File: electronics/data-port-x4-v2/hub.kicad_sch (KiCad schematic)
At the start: 41 parts, among them J1 LEAD, Q1 2N7002, Q2 2N7002, Q3 2N7002, U1 USB2517I-JZX, U2 TCA6408ARGTR, U3 AP2114H-3.3TRG1, U4 H5VU25UC, U6 TCA6408ARGTR, Y1 X322524MSB4SI

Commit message: DATA x4 v2: D2 holds the co-processor in reset with the hub (schematic review S2)
With CFG_SEL 000 the USB2517 samples each downstream D+ / D- as a
port-disable strap when RESET_N rises, and one high line disables the
port (DS00001598C Table 5-1 p.10, checked by the user): the RP2354B's
D+ pull-up on port 5 must not be up by then.

- D2, one Schottky of a BAT54S (C7420333, preferred, no fee; VF <= 240 mV
  at 0.1 mA, <= 320 mV at 1 mA) from CP_RUN to HUB_RST_N, on both
  variants (its second diode open).  RUN sits at ~0.3 V while RESET_N is
  low (R25's ~0.33 mA), under the RP2350's VIL 0.8 V.
- R25 now also charges C6: the hub's reset to VIH 2.0 V goes from ~9.3 to
  ~4.6-5 ms, >> the 1 us minimum; RESET_N stays under VIL through a 3.3 V
  rise of up to ~1.3 ms (DS Note 8-1).
- electronics.md: a self-powered DUT attached during the hub's reset
  loses its port until the next hub reset; CFG_SEL 110 (internal
  defaults, straps off) studied as a way out, not applied, pending the
  user's reading (datasheet audit U11, U12).
- Placed and routed from the vetted routing as a seed, tidy pass, DRC and
  ERC clean; schematics, BOMs, CPL, Gerbers, panel, renders, GLBs.
- bom.py: the BAT54S as added since the panel's quote ($207.89 for 2).

Co-Authored-By: Claude Opus 5.5 <noreply@anthropic.com>
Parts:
- added D2: BAT54S, Package_TO_SOT_SMD:SOT-23, symbol Diode:BAT54S
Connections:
- net HUB_RST_N: now also D2.3 (COM)
- new net CP_RUN: D2.1 (A)
- no-connect marks 29 -> 30
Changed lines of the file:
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@@
 	)
 	(symbol
+		(lib_id "Diode:BAT54S")
+		(at 254 254 90)
+		(unit 1)
+		(exclude_from_sim no)
+		(in_bom yes)
+		(on_board yes)
+		(dnp no)
+		(fields_autoplaced yes)
+		(property "Reference" "D2"
+			(at 261.13 252.73 90)
+			(effects
+				(font
+					(size 1.27 1.27)
+				)
+			)
+		)
+		(property "Value" "BAT54S"
+			(at 263.23 255.27 90)
+			(effects
+				(font
+					(size 1.27 1.27)
+				)
+			)
+		)
+		(property "Footprint" "Package_TO_SOT_SMD:SOT-23"
+			(at 254 254 0)
+			(effects
+				(font
+					(size 1.27 1.27)
+				)
+				(hide yes)
+			)
+		)
+		(property "Datasheet" ""
+			(at 254 254 0)
+			(effects
+				(font
+					(size 1.27 1.27)
+				)
+				(hide yes)
+			)
+		)
+		(property "Description" "dual Schottky in series: clamps a line to GND and +3V3"
+			(at 254 254 0)
+			(effects
+				(font
+					(size 1.27 1.27)
+				)
+				(hide yes)
+			)
+		)
+		(property "MPN" "BAT54S"
+			(at 254 254 0)
+			(effects
+				(font
+					(size 1.27 1.27)
+				)
+				(hide yes)
+			)
+		)
+		(property "Manufacturer" "hongjiacheng"
+			(at 254 254 0)
+			(effects
+				(font
+					(size 1.27 1.27)
+				)
+				(hide yes)
+			)
+		)
+		(property "LCSC" "C7420333"
+			(at 254 254 0)
+			(effects
+				(font
+					(size 1.27 1.27)
+				)
+				(hide yes)
+			)
+		)
+		(pin "1"
+		)
+		(pin "2"
+		)
+		(pin "3"
+		)
+		(instances
+			(project "data-port-x4-v2"
+				(path "/6eede3c9-04e8-5df8-9dbf-dd766ca3200a/45a04347-8732-5237-9e3b-340287b3f578"
+					(reference "D2")
+					(unit 1)
+				)
+			)
+		)
+	)
+	(wire
+		(pts
+			(xy 254 261.62)
+			(xy 254 264.16)
+		)
+		(stroke
+			(width 0)
+			(type default)
+		)
+	)
+	(global_label "CP_RUN"
+		(shape bidirectional)
+		(at 254 264.16 270)
+		(fields_autoplaced yes)
+		(effects
+			(font
+				(size 1.27 1.27)
+			)
+			(justify right)
+		)
+		(property "Intersheetrefs" "${INTERSHEET_REFS}"
+			(at 254 264.16 0)
+			(effects
+				(font
+					(size 1.27 1.27)
+				)
+				(justify right)
+				(hide yes)
+			)
+		)
+	)
+	(no_connect
+		(at 254 246.38)
+	)
+	(wire
+		(pts
+			(xy 259.08 254)
+			(xy 261.62 254)
+		)
+		(stroke
+			(width 0)
+			(type default)
+		)
+	)
+	(label "HUB_RST_N"
+		(at 261.62 254 0)
+		(fields_autoplaced yes)
+		(effects
+			(font
+				(size 1.27 1.27)
+			)
+			(justify left bottom)
+		)
+	)
+	(symbol
 		(lib_id "Device:R")
 		(at 254 233.68 0)
@@
 		)
 	)
-	(text_box "Hub straps: CFG_SEL[2:0] = 000 (internal default, strap options on), NON_REM 00, GANG_EN 0 (ports\n  switched one by one: here by the expanders), BOOST 00, PRT_SWP 0000000; ports 6 and 7 declared but\n  unused (cosmetic).  On purpose: PRTPWR unused and OCS_N on their pull-ups (the node switches each port\n  and reads its FAULT_N through the expanders); VBUS_DET on 3.3 V (self-powered hub).\nHub port n = USB-C n (busid 1-1.n) for n = 1–4; port 5 = the co-processor.\nExpander pins are inputs at power-up; the EN pull-downs keep every port off until the node writes.\nINT (J1.1 → the node's IO4): both expanders' INT and the four INA226 ALERTs, open drain, wired-OR, through Q3.\nI²C and INT: the node's pull-ups on LEAD_*, 4.7k / 4.7k / 10k here; with DUT_5V off the chips here lose\n  their registers: the node sets them up again after each DUT_5V on, and leaves this board's addresses alone while off.\nJ1 (through-hole) stands on the rear face: soldered by hand (the PCBA places the front face only)."
+	(text_box "Hub straps: CFG_SEL[2:0] = 000 (internal default, strap options on), NON_REM 00, GANG_EN 0 (ports\n  switched one by one: here by the expanders), BOOST 00, PRT_SWP 0000000; ports 6 and 7 declared but\n  unused (cosmetic).  On purpose: PRTPWR unused and OCS_N on their pull-ups (the node switches each port\n  and reads its FAULT_N through the expanders); VBUS_DET on 3.3 V (self-powered hub).\nHub port n = USB-C n (busid 1-1.n) for n = 1–4; port 5 = the co-processor.\nD+ / D− of each port are straps at RESET_N's rise (one high line disables the port): D2 holds the\n  co-processor in reset with the hub; a self-powered DUT on a port then loses it until the next hub reset.\nExpander pins are inputs at power-up; the EN pull-downs keep every port off until the node writes.\nINT (J1.1 → the node's IO4): both expanders' INT and the four INA226 ALERTs, open drain, wired-OR, through Q3.\nI²C and INT: the node's pull-ups on LEAD_*, 4.7k / 4.7k / 10k here; with DUT_5V off the chips here lose\n  their registers: the node sets them up again after each DUT_5V on, and leaves this board's addresses alone while off.\nJ1 (through-hole) stands on the rear face: soldered by hand (the PCBA places the front face only)."
 		(exclude_from_sim no)
 		(at 15.24 279.4 0)
-		(size 558.8 26.67)
+		(size 558.8 31.75)
 		(margins 1.5 1.5 1.5 1.5)
 		(stroke

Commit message: DATA x4 v2: datasheet audit fixes 1-9, conservative options, CFG_SEL 110
The DATA x4 v2 datasheet audit's fixes, approved by the user, plus the
conservative options that close U2, U8, U9 and U10:

- Core regulator (fixes 1-3).
  - L1 on a polarity-marked land: bench:L_Abracon_AOTA-B201610, RP's
    0.7 x 1.7 mm pads, the dot on pad 1 = +1V1 (U1's answer).
  - The block is Raspberry Pi's RP2350B Minimal R4-S1 one, turned 180
    degrees with U11, at their coordinates.  CIN and COUT sit on RP's
    0402 land (bench:C_0402_1005Metric_RP), so LX runs 0.3 mm between
    them.
  - Copper: their F.Cu areas (LX, +1V1 with the two V_OUT vias, PGND
    with its two vias, VIN) and their settings; VREG_FB taken at the
    V_OUT vias; CFILT on its own via.
  - The F.Cu GND pour leaves a hole round the block, so PGND meets the
    main GND only through its two vias.  No copper under LX and L1 on
    In1, In2 and B.Cu.
- Fix 4: C47 (DVDD pin 32) 100 nF -> 4.7 uF.
- Fix 5: R40 47k -> 10k, so GPIO45 stays >= -0.48 V; formula updated.
- Fix 6: UMW MAX809S (U5, C347371) drives the hub's RESET_N in place of
  R2/C6; C6 is its 100 nF.
- Fix 7: two H5VU25UC per port in flow-through.  VREF and RESET/BOOT
  sit at the header's two ends, so one part per end:
  - U108-U408 take VREF (logic only);
  - U109-U409 take RESET_N/BOOT_N with the 1k right behind them, fitted
    on the base too (schematic review N4).
  VREF and ports 1-3's RESET_N are drawn into their ESD pins; all 12
  lines checked in flow-through.
- Fixes 8, 9: the VREF isolation wording and the firmware rule (switches
  open below 0.65 V, in multi-dut-node.md); +5V_MX ~1-4 mA, FB1 and U3
  stale lines gone.
- Conservative options:
  - U2: R10 1M across XI-XO (C26083);
  - U8: R115-R415 100k in series with GPIO40-43;
  - U9: R11, R12 10k on the TCA6408A RESETs;
  - U10: C7, C8 4.7 uF.
- Hub on CFG_SEL 110, internal defaults with straps disabled (U11, U12
  answered by the user).  CFG_SEL1 and CFG_SEL2 pull up through their
  RN2/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
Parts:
- removed D2: BAT54S, Package_TO_SOT_SMD:SOT-23, symbol Diode:BAT54S
- removed R2: 10k, Resistor_SMD:R_0402_1005Metric, symbol Device:R
- added R10: 1M, Resistor_SMD:R_0402_1005Metric, symbol Device:R
- added R11, R12: 10k, Resistor_SMD:R_0402_1005Metric, symbol Device:R
- added U5: MAX809S, Package_TO_SOT_SMD:SOT-23, symbol Power_Supervisor:LM809
- C6: value 1u -> 100n; LCSC C52923 -> C1525; MPN CL05A105KA5NQNC -> CL05B104KO5NNNC
- C7, C8: value 1u -> 4.7u; LCSC C52923 -> C23733; MPN CL05A105KA5NQNC -> CL05A475MP5NRNC
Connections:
- net +3V3: now also C6.1, RN2.8 (R1.2), RN3.8 (R1.2), R11.1, R12.1, U5.3 (VCC); no longer U2.1 (~{RESET}), U6.1 (~{RESET})
- net GND: now also U5.1 (GND); no longer RN2.8 (R1.2), RN3.8 (R1.2)
- net HUB_RST_N: now also U5.2 (~{RESET}); no longer C6.1
- net XI: now also R10.2
- net XO: now also R10.1
- new net EXP1_RST_N: R11.2, U2.1 (~{RESET})
- new net EXP2_RST_N: R12.2, U6.1 (~{RESET})
- no-connect marks 30 -> 29
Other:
- note added: "USB2517I hub, CFG_SEL 110 (internal default configuration, straps disabled), 24 MHz crystal"
- note removed: "USB2517I hub on its straps (CFG_SEL 000: internal default, straps on), 24 MHz crystal"
- moved on the sheet: C6

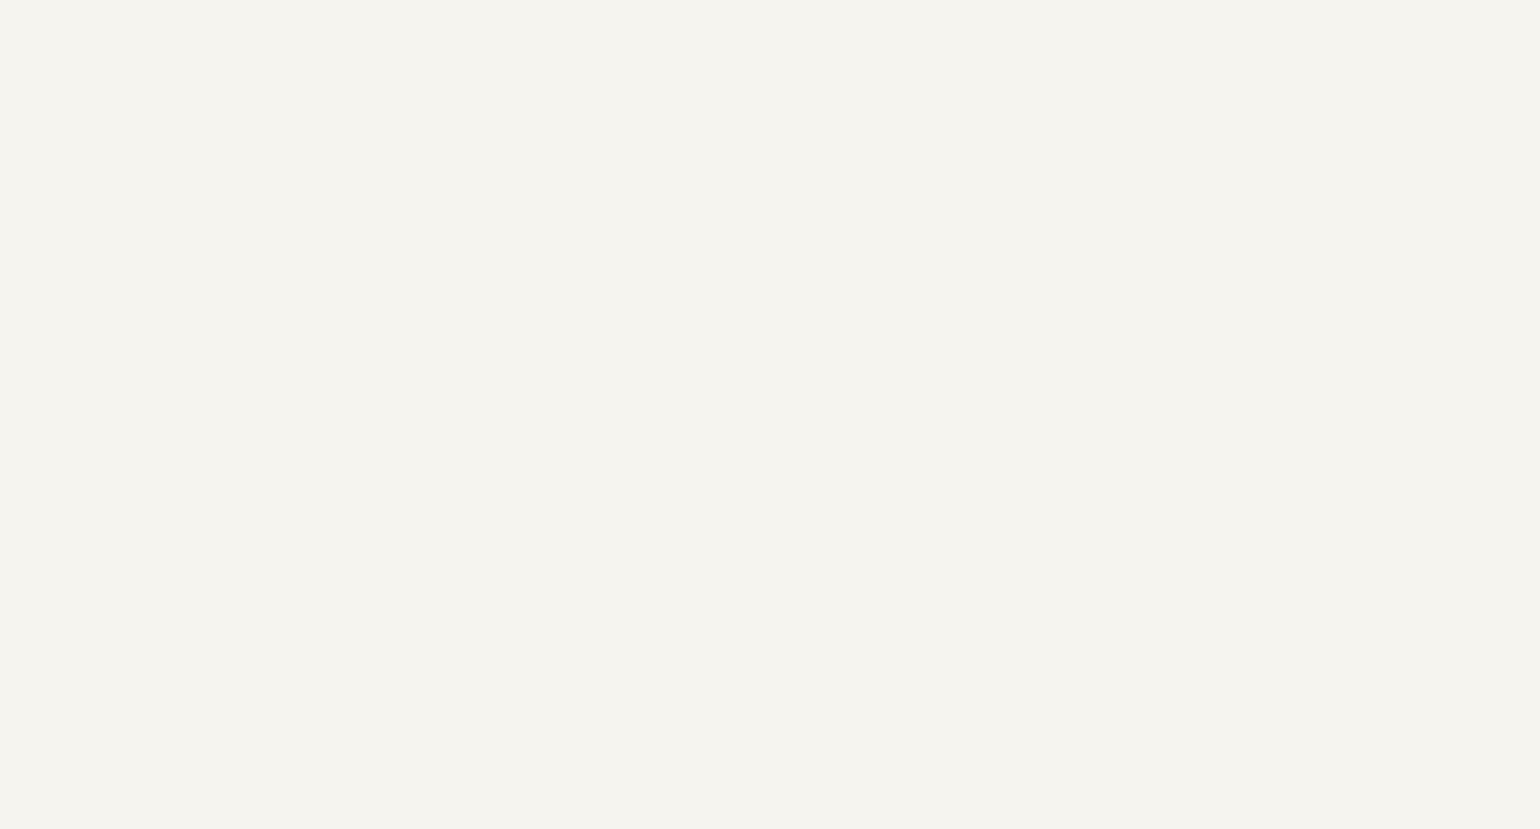
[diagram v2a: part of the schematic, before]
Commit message: DATA x4 v2: 32 labelled bring-up test points on the rear face
Eve's DFT rule on the DATA x4 v2.  Bare pads on B.Cu, mask open, no
paste, out of the BOM and the CPL (no part, no fee).  Each is named on
B.SilkS.  Supplies and GND are 1.5 mm, signals 1.0 mm (main's
"testpad1").  One table in design.py (TPS) holds every position, and
each sheet places its own.

- Co-processor row along the top edge: BOOT, RUN, SWDIO, SWCLK, GND,
  +3V3_CP.  SWD moves here from the front face.  +1V1 sits under the
  chip, on its own rear track.
- Matrix, left column: DAT, CK, STB2, GND, -5V, +5V_MX, GND; STB1 and
  MX RST on their own rear tracks.
- Supplies by the LDO: +3V3, GND, the lead's +5V.
- Hub: HUB RST, GND, 1V8.  Below J1: INT, SDA, SCL (the board side of
  the lead's isolation) and GND.
- Each port's FAULT_N (TP101-TP401) on its own rear track, and a GND by
  each pair's expander.
- Left out: VREF, RESET_N and BOOT_N (on the headers), the lead's lines
  (on J1) and the USB pairs.
- The logic's pads are marked LOGIC ONLY: the base leaves those parts
  off, so they float there.

Every pad is more than 2 mm from the THT pads and from J1, and clear of
the cradle ends, the push band and the notches.  The closest are TP23,
2.0 mm from J1's courtyard, and TP27, 2.1 mm from J101.

Routing: the old routing is seeded as protected wiring, so Freerouting
only adds the new links.  Where it gave up, the pad sits on a rear track
of its own net, or a short drawn link joins it (RUN onto CP_RUN's track,
+3V3_CP through a via to FB2).  The import's tidy pass is applied.

Checks: ERC 0, DRC 0 errors, unconnected 0, parity 0.  The 4
silk_over_copper warnings are the same on main.  Flow-through ESD check
BAD 0.  The fab outputs, panel, renders and GLBs are regenerated; the
BOM and CPL are unchanged.  docs/electronics.md lists the points, and
the "Test pads" table gains the board.

Co-Authored-By: Claude Opus 5.5 <noreply@anthropic.com>
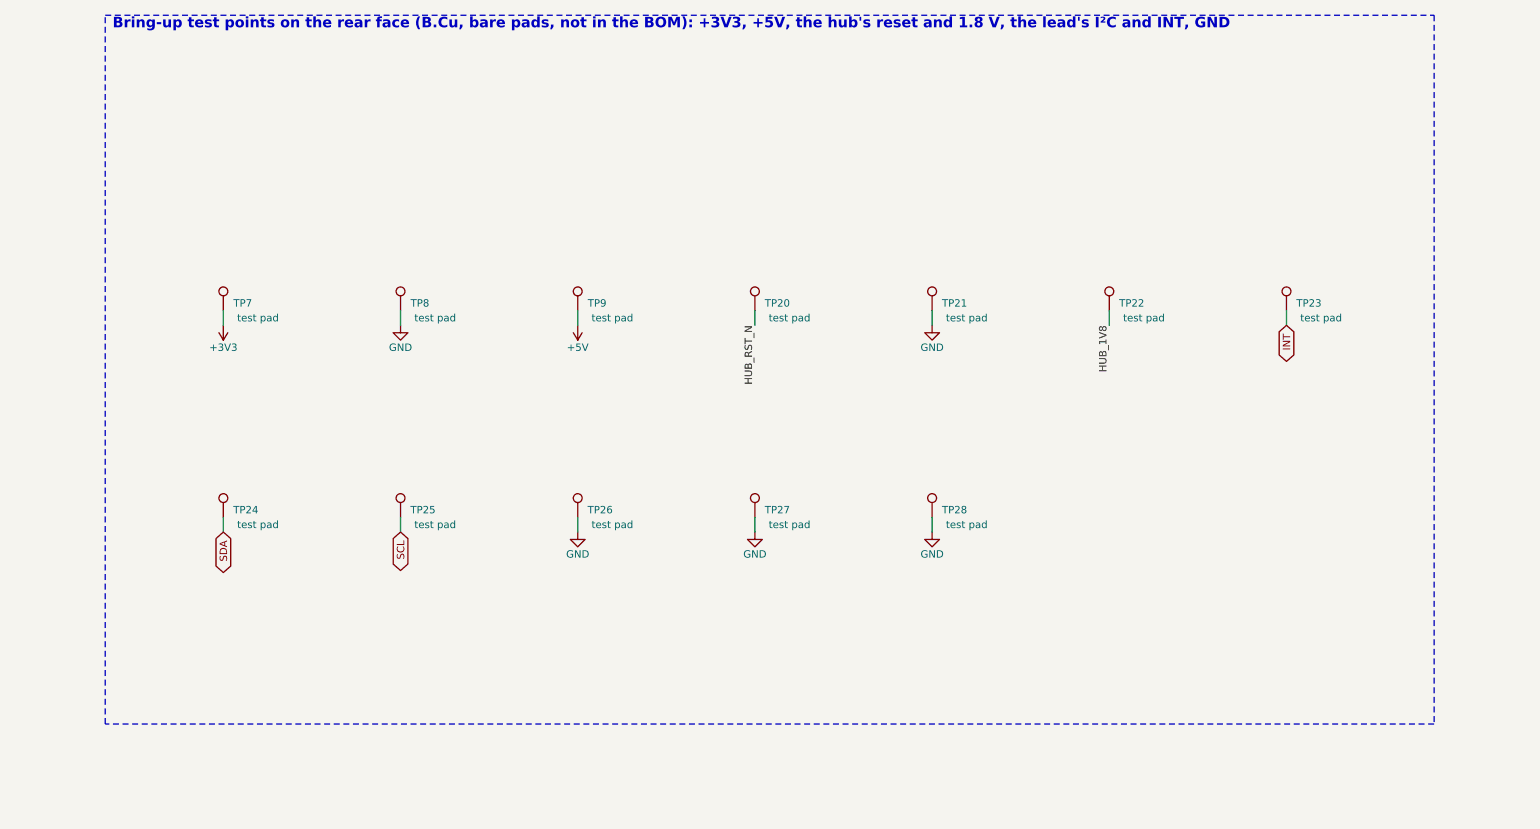
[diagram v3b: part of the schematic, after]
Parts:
- added TP20, TP23, TP24, TP25: test pad, TestPoint:TestPoint_Pad_D1.0mm, symbol Connector:TestPoint
- added TP21, TP22, TP26, TP27, TP28, TP7, TP8, TP9: test pad, TestPoint:TestPoint_Pad_D1.5mm, symbol Connector:TestPoint
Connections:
- net +3V3: now also TP7.1
- net +5V: now also TP9.1
- net GND: now also TP21.1, TP26.1, TP27.1, TP28.1, TP8.1
- net HUB_1V8: now also TP22.1
- net HUB_RST_N: now also TP20.1
- net INT: now also TP23.1
- net SCL: now also TP25.1
- net SDA: now also TP24.1
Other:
- note added: "Bring-up test points on the rear face (B.Cu, bare pads, not in the BOM): +3V3, +5V, the hub's reset and 1.8 V, the lead's I²C and INT, GND"

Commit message: DATA x4 v2: nine vias under the hub's exposed pad, its paste between them
The USB2517I's 4.7 mm exposed pad, its GND and its heat path (about
1.1 W with four High-Speed ports busy), went down one via.  It now takes
a 3 x 3 grid of 0.5 / 0.3 mm GND vias at 1.2 mm into In1.  The stock
footprint's nine 1.26 mm paste windows would sit on those open holes, so
the hub uses bench:QFN-64-1EP_9x9mm_P0.5mm_EP4.7x4.7mm_Paste4x4
(footprints.py): the stock land with 16 paste windows, 0.85 mm square
with 0.3 mm corners, between the vias, 0.12 mm from each ring, 47 % of
the pad.  The stock _ThermalVias variant's 0.2 mm holes are under the
boards' 0.3 mm minimum.  Nothing else moves; the BOMs carry the new
footprint name.

Co-Authored-By: Claude Opus 5.5 <noreply@anthropic.com>
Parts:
- U1: footprint Package_DFN_QFN:QFN-64-1EP_9x9mm_P0.5mm_EP4.7x4.7mm -> bench:QFN-64-1EP_9x9mm_P0.5mm_EP4.7x4.7mm_Paste4x4
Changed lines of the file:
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@@
 			)
 		)
-		(property "Footprint" "Package_DFN_QFN:QFN-64-1EP_9x9mm_P0.5mm_EP4.7x4.7mm"
+		(property "Footprint" "bench:QFN-64-1EP_9x9mm_P0.5mm_EP4.7x4.7mm_Paste4x4"
 			(at 314.96 157.48 0)
 			(effects
